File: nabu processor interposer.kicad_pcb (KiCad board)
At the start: 2 copper layers, 123 parts, among them IC1 Z80CPU-DIP-SOCKET, IC2 Aries 40-600-21, IC3 DMA-PLCC-44-CMOS, IC4 DMA-PLCC-44-CMOS, IC5 DMA-PLCC-44-CMOS, IC6 DMA-PLCC-44-CMOS, J1 5V EXTRA, J2 WRITE PROTECT, J3 USB HOST, J4 ETHERNET, U1 LP3963-3.3, U10 SST39SF040, U11 SST39SF040, U12 SST39SF040, U13 74AHC139, U14 74AHC139, U15 74LVC1G04, U16 74LVC1G02, U17 74LVC1G04, U18 74AHC273, U19 74HC245, U2 TXB0108DQSR, U20 74LVC1G32, U21 74LVC1G02, U22 74AHC273, U23 74HC245, U24 74LVC1G02, U25 74AHC273, U26 74HC245, U27 74LVC1G32, U28 74LVC1G02, U29 74AHC273, U3 TXB0108DQSR, U30 74HC245, U31 74LS153, U32 74LS153, U33 74LS153, U34 74LS153, U35 Teensy4.1, U36 TXB0108DQSR, U37 TXB0108DQSR, U38 74VHC9164FT, U39 74VHC9164FT, U4 TXB0108DQSR, U40 74VHC9164FT, U41 TXB0108DQSR, U42 TXB0108DQSR, U43 TXB0108DQSR, U44 74LS139, U45 74LVC1G32, U46 74HC245, U47 74LVC1G32, U48 74AHC273, U49 74HC74, U5 74LVC1G04, U50 74LS157, U51 74LS157, U52 74LS157, U53 74LS157, U54 74HC74, U55 74LS157, U56 74LS157, U57 74LS157, U58 74LS157, U59 74HC688, U6 TXB0108DQSR, U60 74AHC85, U61 74AHC85, U62 74AHC85, U63 74LVC1G10, U64 74LVC1G10, U65 74LVC1G332, U66 74LVC1G332, U67 74LVC1G04, U68 74LVC1G10, U69 74AHC85, U7 AS6C1616, U70 74LVC1G32, U71 74LVC1G04, U72 74AHC85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

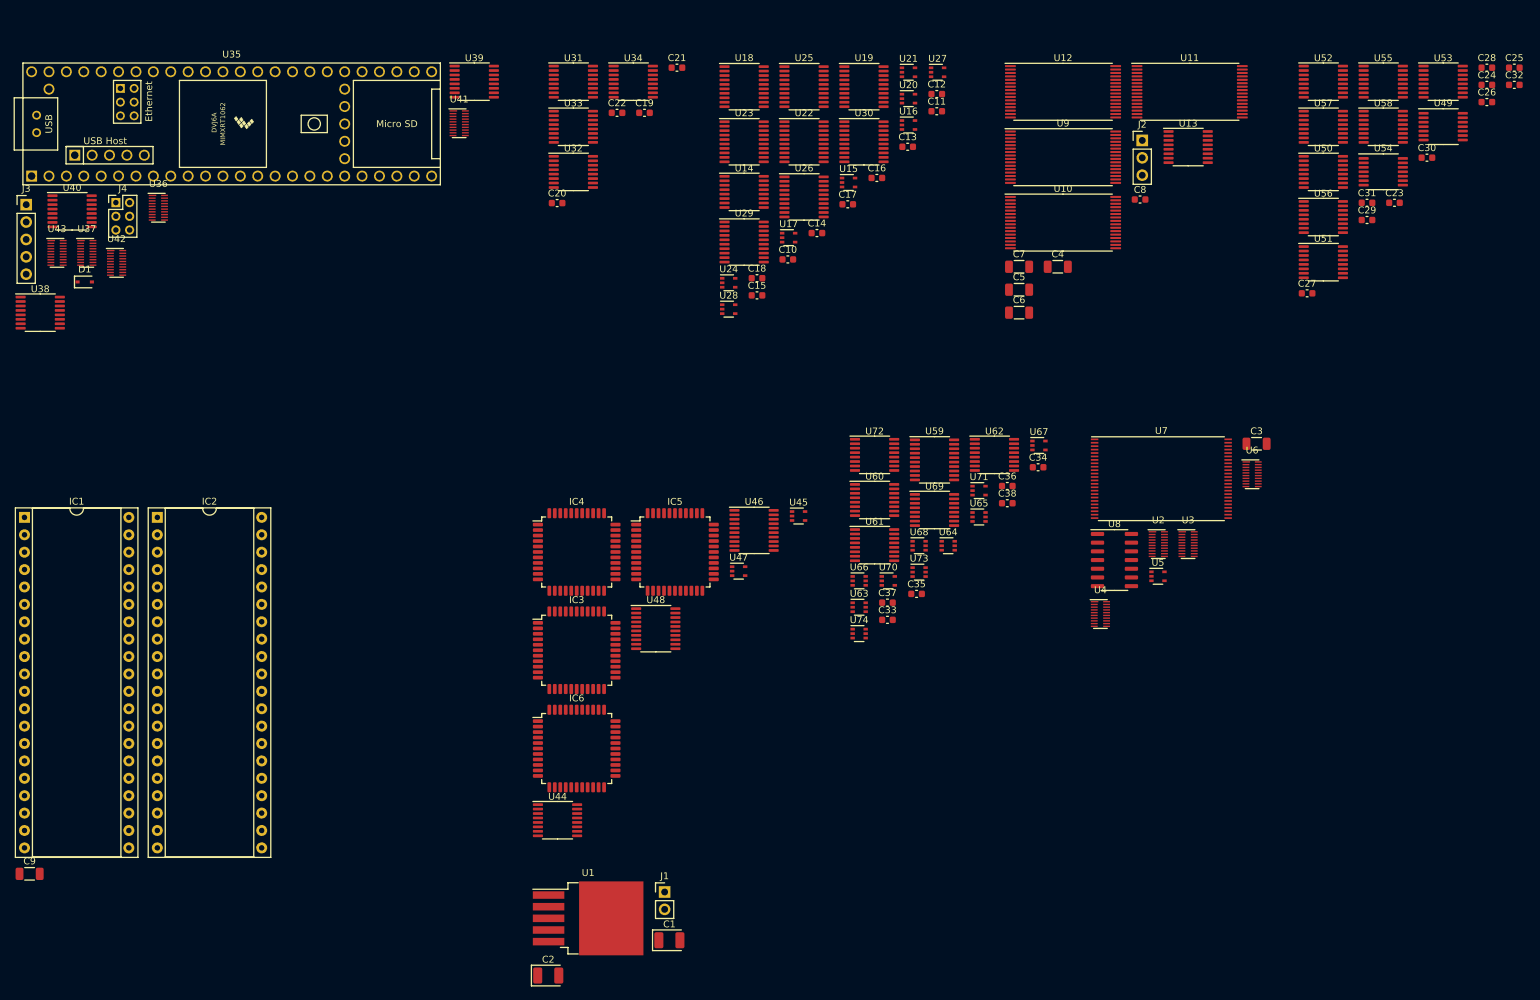
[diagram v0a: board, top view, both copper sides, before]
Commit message: updated 84c10 pinout, apparently never checked for validity.... further simplification of dma and timer system (removed mode 2 interrupt structure, and interrupts in general) cleaned up vhdl code for 1508, still need testing to ensure functionality and that it even fits in the 1508....
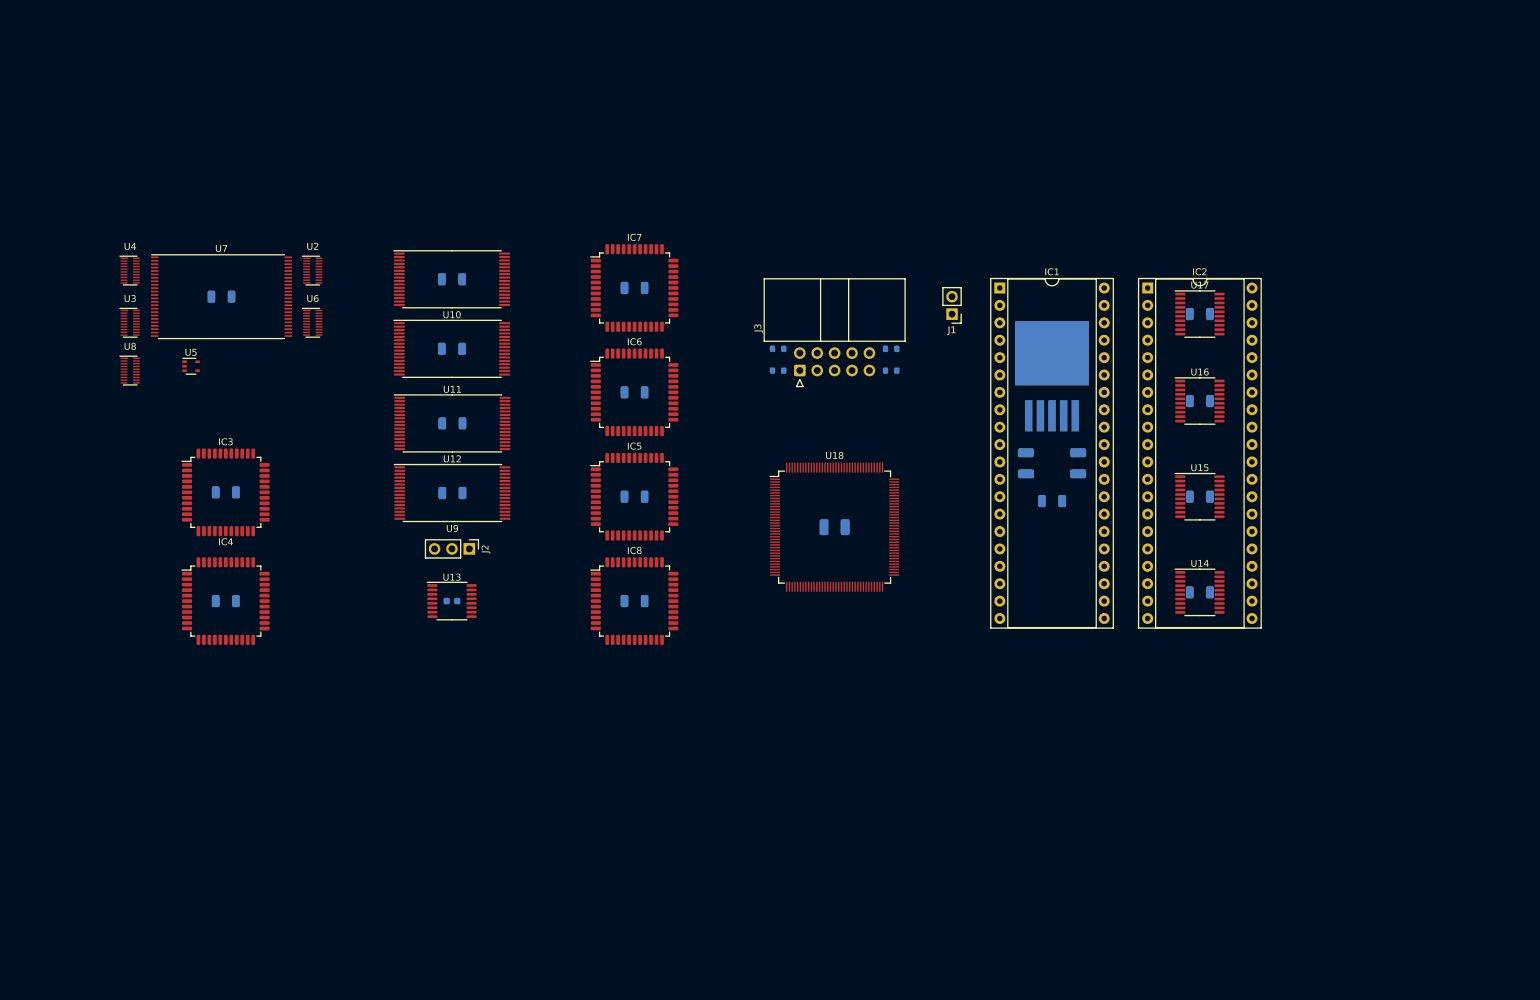
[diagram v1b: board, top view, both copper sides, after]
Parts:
- removed C21, C22, C23, C24, C25, C26, C27, C28, C29, C30, C31, C32, C33, C34, C35, C36, C37, C38: 0U1, Capacitor_SMD:C_0603_1608Metric
- removed D1: BAT48JFILM, Diode_SMD:D_SOD-323
- removed J4: ETHERNET, Connector_PinHeader_2.00mm:PinHeader_2x03_P2.00mm_Vertical
- removed U19, U23, U26, U30, U46: 74HC245, Package_SO:TSSOP-20_4.4x6.5mm_P0.65mm
- removed U20, U27, U45, U47, U70: 74LVC1G32, Package_TO_SOT_SMD:SOT-353_SC-70-5
- removed U21, U24, U28: 74LVC1G02, Package_TO_SOT_SMD:SOT-353_SC-70-5
- removed U22, U25, U29, U48: 74AHC273, Package_SO:TSSOP-20_4.4x6.5mm_P0.65mm
- removed U31, U32, U33, U34: 74LS153, Package_SO:TSSOP-16_4.4x5mm_P0.65mm
- removed U35: Teensy4.1, teensy:Teensy41
- removed U36, U37, U41, U42, U43: TXB0108DQSR, Package_SON:USON-20_2x4mm_P0.4mm
- removed U38, U39, U40: 74VHC9164FT, Package_SO:TSSOP-16_4.4x5mm_P0.65mm
- removed U44: 74LS139, Package_SO:TSSOP-16_4.4x5mm_P0.65mm
- removed U49, U54: 74HC74, Package_SO:TSSOP-14_4.4x5mm_P0.65mm
- removed U50, U51, U52, U53, U55, U56, U57, U58: 74LS157, Package_SO:TSSOP-16_4.4x5mm_P0.65mm
- removed U59: 74HC688, Package_SO:TSSOP-20_4.4x6.5mm_P0.65mm
- removed U60, U61, U62, U69, U72: 74AHC85, Package_SO:TSSOP-16_4.4x5mm_P0.65mm
- removed U63, U64, U68: 74LVC1G10, Package_TO_SOT_SMD:SOT-363_SC-70-6
- removed U65, U66, U73, U74: 74LVC1G332, Package_TO_SOT_SMD:SOT-363_SC-70-6
- removed U67, U71: 74LVC1G04, Package_TO_SOT_SMD:SOT-353_SC-70-5
- added IC7: DMA-PLCC-44-CMOS, Package_QFP:LQFP-44_10x10mm_P0.8mm, F.Cu at (134.6, 62.2)
- added IC8: DMA-PLCC-44-CMOS, Package_QFP:LQFP-44_10x10mm_P0.8mm, F.Cu at (134.6, 108.0)
- added R1: 4K7, Resistor_SMD:R_0603_1608Metric, B.Cu at (155.6, 74.3)
- added R2: 4K7, Resistor_SMD:R_0603_1608Metric, B.Cu at (172.1, 71.1)
- added R3: 4K7, Resistor_SMD:R_0603_1608Metric, B.Cu at (172.1, 74.3)
- added R4: 10K, Resistor_SMD:R_0603_1608Metric, B.Cu at (155.6, 71.1)
- C1, C2, C3, C4, C5, C6, C7, C8, U1: moved to B.Cu
- C10, C14, C15, C17, C18, C19, C20: value 0U1 -> 1U; footprint Capacitor_SMD:C_0603_1608Metric -> Capacitor_SMD:C_1206_3216Metric; moved to B.Cu
- C11, C12, C13: footprint Capacitor_SMD:C_0603_1608Metric -> Capacitor_SMD:C_1206_3216Metric; moved to B.Cu
- C16: value 0U1 -> 10U TANT; footprint Capacitor_SMD:C_0603_1608Metric -> Capacitor_Tantalum_SMD:CP_EIA-3528-15_AVX-H; moved to B.Cu
- C9: value 1U -> 0U1; moved to B.Cu
- IC1: value Z80CPU-DIP-SOCKET -> Aries 40-600-21
- IC2: value Aries 40-600-21 -> Z80CPU-DIP-SOCKET
- IC3, IC4: value DMA-PLCC-44-CMOS -> CTC-QFP-44
- J3: value USB HOST -> AVR-JTAG-10; footprint Connector_PinHeader_2.54mm:PinHeader_1x05_P2.54mm_Vertical -> Connector_IDC:IDC-Header_2x05_P2.54mm_Horizontal
- U14: value 74AHC139 -> 74HC245; footprint Package_SO:TSSOP-16_4.4x5mm_P0.65mm -> Package_SO:TSSOP-20_4.4x6.5mm_P0.65mm
- U15, U17: value 74LVC1G04 -> 74HC245; footprint Package_TO_SOT_SMD:SOT-353_SC-70-5 -> Package_SO:TSSOP-20_4.4x6.5mm_P0.65mm
- U16: value 74LVC1G02 -> 74HC245; footprint Package_TO_SOT_SMD:SOT-353_SC-70-5 -> Package_SO:TSSOP-20_4.4x6.5mm_P0.65mm
- U18: value 74AHC273 -> ATF1508-100; footprint Package_SO:TSSOP-20_4.4x6.5mm_P0.65mm -> Package_QFP:TQFP-144_16x16mm_P0.4mm
- U8: value TXB0104D -> TXB0108DQSR; footprint Package_SO:SOIC-14_3.9x8.7mm_P1.27mm -> Package_SON:USON-20_2x4mm_P0.4mm
- moved C9 175.8 mm to (217.2, 106.7), turned to 180 degrees
- moved U3 157.8 mm to (61.0, 67.3)
- moved C3 152.7 mm to (74.3, 63.5), turned to 180 degrees
- moved U4 150.3 mm to (61.0, 59.7)
- moved IC2 148.4 mm to (209.5, 62.2)
- moved U8 146.4 mm to (61.0, 74.3)
- moved IC1 146.3 mm to (188.0, 62.2)
- moved U5 144.5 mm to (69.8, 73.7)
- moved U7 139.8 mm to (74.3, 63.5)
- moved U6 138.9 mm to (87.6, 67.3)
- moved U2 129.8 mm to (87.6, 59.7)
- moved U13 126.3 mm to (108.0, 108.0)
- moved U11 118.1 mm to (108.0, 82.0)
- moved C8 116.3 mm to (108.0, 108.0), turned to 180 degrees
- moved J3 115.5 mm to (158.8, 74.3), turned to 90 degrees
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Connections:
- net /ROM/~{ROMEN0} renamed /ROM/~{ROM0}
- net /ROM/~{ROMEN_{1}} renamed /ROM/~{ROM_{1}}
- net /ROM/~{ROMEN_{2}} renamed /ROM/~{ROM_{2}}
- net /ROM/~{ROMEN_{3}} renamed /ROM/~{ROM_{3}}
- IC1 pad 1: /BRAINS/AB11 -> /BRAINS/XAB11
- IC1 pad 10: /BRAINS/DB6 -> /BRAINS/EDB6
- IC1 pad 12: /BRAINS/DB2 -> /BRAINS/EDB2
- IC1 pad 13: /BRAINS/DB7 -> /BRAINS/EDB7
- IC1 pad 14: /BRAINS/DB0 -> /BRAINS/EDB0
- IC1 pad 15: /BRAINS/DB1 -> /BRAINS/EDB1
- IC1 pad 17: unconnected-(IC1-Pad17) -> /BRAINS/~{NMI}
- IC1 pad 18: unconnected-(IC1-Pad18) -> /BRAINS/~{HALT}
- IC1 pad 19: /BRAINS/~{MREQ} -> /BRAINS/~{XMREQ}
- IC1 pad 2: /BRAINS/AB12 -> /BRAINS/XAB12
- IC1 pad 20: /BRAINS/~{IOREQ} -> /BRAINS/~{XIOREQ}
- IC1 pad 21: /BRAINS/~{RD} -> /BRAINS/~{XRD}
- IC1 pad 22: /BRAINS/~{WR} -> /BRAINS/~{XWR}
- IC1 pad 24: unconnected-(IC1-Pad24) -> /BRAINS/~{WAIT}
- IC1 pad 27: /BRAINS/~{M1} -> /BRAINS/~{XM1}
- IC1 pad 28: Net-(IC1-Pad28) -> /BRAINS/~{RFSH}
- IC1 pad 3: /BRAINS/AB13 -> /BRAINS/XAB13
- IC1 pad 30: /BRAINS/AB0 -> /BRAINS/XAB0
- IC1 pad 31: /BRAINS/AB1 -> /BRAINS/XAB1
- IC1 pad 32: /BRAINS/AB2 -> /BRAINS/XAB2
- IC1 pad 33: /BRAINS/AB3 -> /BRAINS/XAB3
- IC1 pad 34: /BRAINS/AB4 -> /BRAINS/XAB4
- IC1 pad 35: /BRAINS/AB5 -> /BRAINS/XAB5
- IC1 pad 36: /BRAINS/AB6 -> /BRAINS/XAB6
- IC1 pad 37: /BRAINS/AB7 -> /BRAINS/XAB7
- IC1 pad 38: /BRAINS/AB8 -> /BRAINS/XAB8
- IC1 pad 39: /BRAINS/AB9 -> /BRAINS/XAB9
- IC1 pad 4: /BRAINS/AB14 -> /BRAINS/XAB14
- IC1 pad 40: /BRAINS/AB10 -> /BRAINS/XAB10
- IC1 pad 5: /BRAINS/AB15 -> /BRAINS/XAB15
- IC1 pad 7: /BRAINS/DB4 -> /BRAINS/EDB4
- IC1 pad 8: /BRAINS/DB3 -> /BRAINS/EDB3
- IC1 pad 9: /BRAINS/DB5 -> /BRAINS/EDB5
- IC2 pad 28: Net-(IC1-Pad28) -> /BRAINS/~{RFSH}
- IC3 pad 1: /DECODE/AB5 -> /BRAINS/DB0
- IC3 pad 10: /DECODE/~{PORT_{4}RD} -> /BRAINS/DB6
- IC3 pad 11: /BRAINS/~{IOREQ} -> unconnected-(IC3-Pad11)
- IC3 pad 12: /BRAINS/~{RST} -> /BRAINS/DB7
- IC3 pad 13: +5V -> GND
- IC3 pad 14: /BRAINS/~{MREQ} -> /BRAINS/~{RD}
- IC3 pad 15: Net-(IC3-Pad15) -> unconnected-(IC3-Pad15)
- IC3 pad 16: /BRAINS/~{BUSAK} -> /DMA/RDY0
- IC3 pad 17: /BRAINS/~{BUSREQ} -> unconnected-(IC3-Pad17)
- IC3 pad 18: /DMA/~{DMASEL_{0}} -> /DMA/RDY1
- IC3 pad 19: /DECODE/AB15 -> Net-(IC3-Pad19)
- IC3 pad 2: /DECODE/AB4 -> /BRAINS/DB1
- IC3 pad 20: /DECODE/AB14 -> unconnected-(IC3-Pad20)
- IC3 pad 21: /DECODE/AB13 -> /BRAINS/~{IOREQ}
- IC3 pad 22: /DECODE/AB12 -> unconnected-(IC3-Pad22)
- IC3 pad 23: /DECODE/AB11 -> unconnected-(IC3-Pad23)
- IC3 pad 24: /DECODE/AB10 -> unconnected-(IC3-Pad24)
- IC3 pad 25: /DECODE/AB9 -> +5V
- IC3 pad 26: /DECODE/AB8 -> unconnected-(IC3-Pad26)
- IC3 pad 27: /DMA/DMARDY_{0} -> /BRAINS/~{M1}
- IC3 pad 29: unconnected-(IC3-Pad29) -> /BRAINS/CLK
- IC3 pad 3: /DECODE/AB3 -> /BRAINS/DB2
- IC3 pad 30: /BRAINS/~{M1} -> unconnected-(IC3-Pad30)
- IC3 pad 31: /DMA/DB7 -> /GLUE/~{TI0}
- IC3 pad 32: /DMA/DB5 -> /BRAINS/DB3
- IC3 pad 33: /DMA/DB6 -> /BRAINS/AB1
- IC3 pad 34: GND -> unconnected-(IC3-Pad34)
- IC3 pad 35: /DMA/DB4 -> /BRAINS/AB0
- IC3 pad 36: /DMA/DB3 -> Net-(IC3-Pad19)
- IC3 pad 37: /DMA/DB2 -> /BRAINS/CLK
- IC3 pad 38: /DMA/DB1 -> unconnected-(IC3-Pad38)
- IC3 pad 39: /DMA/DB0 -> unconnected-(IC3-Pad39)
- IC3 pad 4: /DECODE/AB2 -> /BRAINS/~{RST}
- IC3 pad 40: Net-(IC3-Pad40) -> /BRAINS/CLK
- IC3 pad 41: /BRAINS/~{INT} -> /BRAINS/CLK
- IC3 pad 42: (no net) -> unconnected-(IC3-Pad42)
- IC3 pad 43: /DECODE/AB7 -> +5V
- IC3 pad 44: /DECODE/AB6 -> unconnected-(IC3-Pad44)
- IC3 pad 5: /DECODE/AB1 -> unconnected-(IC3-Pad5)
- IC3 pad 6: (no net) -> unconnected-(IC3-Pad6)
- IC3 pad 7: /DECODE/AB0 -> unconnected-(IC3-Pad7)
- IC3 pad 8: /BRAINS/CLK -> /BRAINS/DB4
- IC3 pad 9: /DECODE/~{PORT_{4}WR} -> /BRAINS/DB5
- IC4 pad 1: /DECODE/AB5 -> /BRAINS/DB0
- IC4 pad 10: /DECODE/~{PORT_{4}RD} -> /BRAINS/DB6
- IC4 pad 11: /BRAINS/~{IOREQ} -> unconnected-(IC4-Pad11)
- IC4 pad 12: /BRAINS/~{RST} -> /BRAINS/DB7
- IC4 pad 13: +5V -> GND
- IC4 pad 14: /BRAINS/~{MREQ} -> /BRAINS/~{RD}
- IC4 pad 15: Net-(IC4-Pad15) -> unconnected-(IC4-Pad15)
- IC4 pad 16: Net-(IC3-Pad15) -> /DMA/RDY2
- IC4 pad 17: /BRAINS/~{BUSREQ} -> unconnected-(IC4-Pad17)
- IC4 pad 18: /DMA/~{DMASEL_{1}} -> /DMA/RDY3
- IC4 pad 19: /DECODE/AB15 -> Net-(IC4-Pad19)
- IC4 pad 2: /DECODE/AB4 -> /BRAINS/DB1
- IC4 pad 20: /DECODE/AB14 -> unconnected-(IC4-Pad20)
- IC4 pad 21: /DECODE/AB13 -> /BRAINS/~{IOREQ}
- IC4 pad 22: /DECODE/AB12 -> unconnected-(IC4-Pad22)
- IC4 pad 23: /DECODE/AB11 -> unconnected-(IC4-Pad23)
- IC4 pad 24: /DECODE/AB10 -> unconnected-(IC4-Pad24)
- IC4 pad 25: /DECODE/AB9 -> +5V
- IC4 pad 26: /DECODE/AB8 -> unconnected-(IC4-Pad26)
- IC4 pad 27: /DMA/DMARDY_{1} -> /BRAINS/~{M1}
- IC4 pad 29: unconnected-(IC4-Pad29) -> /BRAINS/CLK
- IC4 pad 3: /DECODE/AB3 -> /BRAINS/DB2
- IC4 pad 30: /BRAINS/~{M1} -> unconnected-(IC4-Pad30)
- IC4 pad 31: /DMA/DB7 -> /GLUE/~{TI1}
- IC4 pad 32: /DMA/DB5 -> /BRAINS/DB3
- IC4 pad 33: /DMA/DB6 -> /BRAINS/AB1
- IC4 pad 34: GND -> unconnected-(IC4-Pad34)
- IC4 pad 35: /DMA/DB4 -> /BRAINS/AB0
- IC4 pad 36: /DMA/DB3 -> Net-(IC4-Pad19)
- IC4 pad 37: /DMA/DB2 -> /BRAINS/CLK
- IC4 pad 38: /DMA/DB1 -> unconnected-(IC4-Pad38)
- IC4 pad 39: /DMA/DB0 -> unconnected-(IC4-Pad39)
- IC4 pad 4: /DECODE/AB2 -> /BRAINS/~{RST}
- IC4 pad 40: Net-(IC4-Pad40) -> /BRAINS/CLK
- IC4 pad 41: /BRAINS/~{INT} -> /BRAINS/CLK
- IC4 pad 42: (no net) -> unconnected-(IC4-Pad42)
- IC4 pad 43: /DECODE/AB7 -> +5V
- IC4 pad 44: /DECODE/AB6 -> unconnected-(IC4-Pad44)
- IC4 pad 5: /DECODE/AB1 -> unconnected-(IC4-Pad5)
- IC4 pad 6: (no net) -> unconnected-(IC4-Pad6)
- IC4 pad 7: /DECODE/AB0 -> unconnected-(IC4-Pad7)
- IC4 pad 8: /BRAINS/CLK -> /BRAINS/DB4
- IC4 pad 9: /DECODE/~{PORT_{4}WR} -> /BRAINS/DB5
- IC5 pad 1: /DECODE/AB5 -> /BRAINS/AB5
- IC5 pad 10: /DECODE/~{PORT_{4}RD} -> /BRAINS/~{RD}
- IC5 pad 16: Net-(IC4-Pad15) -> /BRAINS/~{BUSAK}
- IC5 pad 18: /DMA/~{DMASEL_{2}} -> /DMA/~{DMASEL_{0}}
- IC5 pad 19: /DECODE/AB15 -> /BRAINS/AB15
- IC5 pad 2: /DECODE/AB4 -> /BRAINS/AB4
- IC5 pad 20: /DECODE/AB14 -> /BRAINS/AB14
- IC5 pad 21: /DECODE/AB13 -> /BRAINS/AB13
- IC5 pad 22: /DECODE/AB12 -> /BRAINS/AB12
- IC5 pad 23: /DECODE/AB11 -> /BRAINS/AB11
- IC5 pad 24: /DECODE/AB10 -> /BRAINS/AB10
- IC5 pad 25: /DECODE/AB9 -> /BRAINS/AB9
- IC5 pad 26: /DECODE/AB8 -> /BRAINS/AB8
- IC5 pad 27: /DMA/DMARDY_{2} -> /DMA/RDY0
- IC5 pad 3: /DECODE/AB3 -> /BRAINS/AB3
- IC5 pad 31: /DMA/DB7 -> /BRAINS/DB7
- IC5 pad 32: /DMA/DB5 -> /BRAINS/DB6
- IC5 pad 33: /DMA/DB6 -> /BRAINS/DB5
- IC5 pad 35: /DMA/DB4 -> /BRAINS/DB4
- IC5 pad 36: /DMA/DB3 -> /BRAINS/DB3
- IC5 pad 37: /DMA/DB2 -> /BRAINS/DB2
- IC5 pad 38: /DMA/DB1 -> /BRAINS/DB1
- IC5 pad 39: /DMA/DB0 -> /BRAINS/DB0
- IC5 pad 4: /DECODE/AB2 -> /BRAINS/AB2
- IC5 pad 40: Net-(IC5-Pad40) -> unconnected-(IC5-Pad40)
- IC5 pad 41: /BRAINS/~{INT} -> unconnected-(IC5-Pad41)
- IC5 pad 42: (no net) -> +5V
- IC5 pad 43: /DECODE/AB7 -> /BRAINS/AB7
- IC5 pad 44: /DECODE/AB6 -> /BRAINS/AB6
- IC5 pad 5: /DECODE/AB1 -> /BRAINS/AB1
- IC5 pad 7: /DECODE/AB0 -> /BRAINS/AB0
- IC5 pad 9: /DECODE/~{PORT_{4}WR} -> /BRAINS/~{WR}
- IC6 pad 1: /DECODE/AB5 -> /BRAINS/AB5
- IC6 pad 10: /DECODE/~{PORT_{4}RD} -> /BRAINS/~{RD}
- IC6 pad 15: unconnected-(IC6-Pad15) -> Net-(IC6-Pad15)
- IC6 pad 18: /DMA/~{DMASEL_{3}} -> /DMA/~{DMASEL_{1}}
- IC6 pad 19: /DECODE/AB15 -> /BRAINS/AB15
- IC6 pad 2: /DECODE/AB4 -> /BRAINS/AB4
- IC6 pad 20: /DECODE/AB14 -> /BRAINS/AB14
- IC6 pad 21: /DECODE/AB13 -> /BRAINS/AB13
- IC6 pad 22: /DECODE/AB12 -> /BRAINS/AB12
- IC6 pad 23: /DECODE/AB11 -> /BRAINS/AB11
- IC6 pad 24: /DECODE/AB10 -> /BRAINS/AB10
- IC6 pad 25: /DECODE/AB9 -> /BRAINS/AB9
- IC6 pad 26: /DECODE/AB8 -> /BRAINS/AB8
- IC6 pad 27: /DMA/DMARDY_{3} -> /DMA/RDY1
- IC6 pad 3: /DECODE/AB3 -> /BRAINS/AB3
- IC6 pad 31: /DMA/DB7 -> /BRAINS/DB7
- IC6 pad 32: /DMA/DB5 -> /BRAINS/DB6
- IC6 pad 33: /DMA/DB6 -> /BRAINS/DB5
- IC6 pad 35: /DMA/DB4 -> /BRAINS/DB4
- IC6 pad 36: /DMA/DB3 -> /BRAINS/DB3
- IC6 pad 37: /DMA/DB2 -> /BRAINS/DB2
- IC6 pad 38: /DMA/DB1 -> /BRAINS/DB1
- IC6 pad 39: /DMA/DB0 -> /BRAINS/DB0
- IC6 pad 4: /DECODE/AB2 -> /BRAINS/AB2
- IC6 pad 41: /BRAINS/~{INT} -> unconnected-(IC6-Pad41)
- IC6 pad 42: (no net) -> +5V
- IC6 pad 43: /DECODE/AB7 -> /BRAINS/AB7
- IC6 pad 44: /DECODE/AB6 -> /BRAINS/AB6
- IC6 pad 5: /DECODE/AB1 -> /BRAINS/AB1
- IC6 pad 7: /DECODE/AB0 -> /BRAINS/AB0
- IC6 pad 9: /DECODE/~{PORT_{4}WR} -> /BRAINS/~{WR}
- J2 pad 1: /BRAINS/~{WR} -> /RAM/~{WR}
- J3 pad 1: Net-(J3-Pad1) -> /GLUE/TCK
- J3 pad 2: Net-(J3-Pad2) -> GND
- J3 pad 3: Net-(J3-Pad3) -> /GLUE/TDO
- J3 pad 4: GND -> +5V
- J3 pad 5: GND -> /GLUE/TMS
- U10 pad 1: /MUX/EAB18 -> /GLUE/EAB18
- U10 pad 10: /MUX/AB2 -> /GLUE/EAB2
- U10 pad 11: /MUX/AB1 -> /GLUE/EAB1
- U10 pad 12: /MUX/AB0 -> /GLUE/EAB0
- U10 pad 13: /DEV PORT/DB0 -> /BRAINS/DB0
- U10 pad 14: /DEV PORT/DB1 -> /BRAINS/DB1
- U10 pad 15: /DEV PORT/DB2 -> /BRAINS/DB2
- U10 pad 17: /DEV PORT/DB3 -> /BRAINS/DB3
- U10 pad 18: /DEV PORT/DB4 -> /BRAINS/DB4
- U10 pad 19: /DEV PORT/DB5 -> /BRAINS/DB5
- U10 pad 2: /MUX/EAB16 -> /GLUE/EAB16
- U10 pad 20: /DEV PORT/DB6 -> /BRAINS/DB6
- U10 pad 21: /DEV PORT/DB7 -> /BRAINS/DB7
- U10 pad 23: /MUX/AB10 -> /GLUE/EAB10
- U10 pad 24: /BRAINS/~{RD} -> /RAM/~{RD}
- U10 pad 25: /MUX/AB11 -> /GLUE/EAB11
- U10 pad 26: /MUX/AB9 -> /GLUE/EAB9
- U10 pad 27: /MUX/AB8 -> /GLUE/EAB8
- U10 pad 28: /MUX/AB13 -> /GLUE/EAB13
- U10 pad 29: /MUX/EAB14 -> /GLUE/EAB14
- U10 pad 3: /MUX/EAB15 -> /GLUE/EAB15
- U10 pad 30: /MUX/EAB17 -> /GLUE/EAB17
- U10 pad 4: /MUX/AB12 -> /GLUE/EAB12
- U10 pad 5: /MUX/AB7 -> /GLUE/EAB7
- U10 pad 6: /MUX/AB6 -> /GLUE/EAB6
- U10 pad 7: /MUX/AB5 -> /GLUE/EAB5
- U10 pad 8: /MUX/AB4 -> /GLUE/EAB4
- U10 pad 9: /MUX/AB3 -> /GLUE/EAB3
- U11 pad 1: /MUX/EAB18 -> /GLUE/EAB18
- U11 pad 10: /MUX/AB2 -> /GLUE/EAB2
- U11 pad 11: /MUX/AB1 -> /GLUE/EAB1
- U11 pad 12: /MUX/AB0 -> /GLUE/EAB0
- U11 pad 13: /DEV PORT/DB0 -> /BRAINS/DB0
- U11 pad 14: /DEV PORT/DB1 -> /BRAINS/DB1
- U11 pad 15: /DEV PORT/DB2 -> /BRAINS/DB2
- U11 pad 17: /DEV PORT/DB3 -> /BRAINS/DB3
- U11 pad 18: /DEV PORT/DB4 -> /BRAINS/DB4
- U11 pad 19: /DEV PORT/DB5 -> /BRAINS/DB5
- U11 pad 2: /MUX/EAB16 -> /GLUE/EAB16
- U11 pad 20: /DEV PORT/DB6 -> /BRAINS/DB6
- U11 pad 21: /DEV PORT/DB7 -> /BRAINS/DB7
- U11 pad 23: /MUX/AB10 -> /GLUE/EAB10
- U11 pad 24: /BRAINS/~{RD} -> /RAM/~{RD}
- U11 pad 25: /MUX/AB11 -> /GLUE/EAB11
- U11 pad 26: /MUX/AB9 -> /GLUE/EAB9
- U11 pad 27: /MUX/AB8 -> /GLUE/EAB8
- U11 pad 28: /MUX/AB13 -> /GLUE/EAB13
- U11 pad 29: /MUX/EAB14 -> /GLUE/EAB14
- U11 pad 3: /MUX/EAB15 -> /GLUE/EAB15
- U11 pad 30: /MUX/EAB17 -> /GLUE/EAB17
- U11 pad 4: /MUX/AB12 -> /GLUE/EAB12
- U11 pad 5: /MUX/AB7 -> /GLUE/EAB7
- U11 pad 6: /MUX/AB6 -> /GLUE/EAB6
- U11 pad 7: /MUX/AB5 -> /GLUE/EAB5
- U11 pad 8: /MUX/AB4 -> /GLUE/EAB4
- U11 pad 9: /MUX/AB3 -> /GLUE/EAB3
- U12 pad 1: /MUX/EAB18 -> /GLUE/EAB18
- U12 pad 10: /MUX/AB2 -> /GLUE/EAB2
- U12 pad 11: /MUX/AB1 -> /GLUE/EAB1
- U12 pad 12: /MUX/AB0 -> /GLUE/EAB0
- U12 pad 13: /DEV PORT/DB0 -> /BRAINS/DB0
- U12 pad 14: /DEV PORT/DB1 -> /BRAINS/DB1
- U12 pad 15: /DEV PORT/DB2 -> /BRAINS/DB2
- U12 pad 17: /DEV PORT/DB3 -> /BRAINS/DB3
- U12 pad 18: /DEV PORT/DB4 -> /BRAINS/DB4
- U12 pad 19: /DEV PORT/DB5 -> /BRAINS/DB5
- U12 pad 2: /MUX/EAB16 -> /GLUE/EAB16
- U12 pad 20: /DEV PORT/DB6 -> /BRAINS/DB6
- U12 pad 21: /DEV PORT/DB7 -> /BRAINS/DB7
- U12 pad 23: /MUX/AB10 -> /GLUE/EAB10
- U12 pad 24: /BRAINS/~{RD} -> /RAM/~{RD}
- U12 pad 25: /MUX/AB11 -> /GLUE/EAB11
- U12 pad 26: /MUX/AB9 -> /GLUE/EAB9
- U12 pad 27: /MUX/AB8 -> /GLUE/EAB8
- U12 pad 28: /MUX/AB13 -> /GLUE/EAB13
- U12 pad 29: /MUX/EAB14 -> /GLUE/EAB14
- U12 pad 3: /MUX/EAB15 -> /GLUE/EAB15
- U12 pad 30: /MUX/EAB17 -> /GLUE/EAB17
- U12 pad 4: /MUX/AB12 -> /GLUE/EAB12
- U12 pad 5: /MUX/AB7 -> /GLUE/EAB7
- U12 pad 6: /MUX/AB6 -> /GLUE/EAB6
- U12 pad 7: /MUX/AB5 -> /GLUE/EAB5
- U12 pad 8: /MUX/AB4 -> /GLUE/EAB4
- U12 pad 9: /MUX/AB3 -> /GLUE/EAB3
- U13 pad 1: /DECODE/~{ROMEN} -> /GLUE/~{ROM}
- U13 pad 10: unconnected-(U13-Pad10) -> /DMA/~{DMASEL_{2}}
- U13 pad 11: unconnected-(U13-Pad11) -> /DMA/~{DMASEL_{1}}
- U13 pad 12: unconnected-(U13-Pad12) -> /DMA/~{DMASEL_{0}}
- U13 pad 13: GND -> /BRAINS/AB1
- U13 pad 14: GND -> /BRAINS/AB0
- U13 pad 15: +5V -> /DMA/~{DMA}
- U13 pad 2: /MUX/EAB20 -> /GLUE/EAB20
- U13 pad 3: /MUX/EAB19 -> /GLUE/EAB19
- U13 pad 9: unconnected-(U13-Pad9) -> /DMA/~{DMASEL_{3}}
- U14 pad 1: Net-(U14-Pad1) -> GND
- U14 pad 10: /MAPPER/~{MAPRD_{2}} -> GND
- U14 pad 11: /MAPPER/~{MAPRD_{1}} -> unconnected-(U14-Pad11)
- U14 pad 12: /MAPPER/~{MAPRD_{0}} -> unconnected-(U14-Pad12)
- U14 pad 13: /MAPPER/AB0 -> unconnected-(U14-Pad13)
- U14 pad 14: /MAPPER/AB1 -> /BRAINS/~{WR}
- U14 pad 15: Net-(U14-Pad15) -> /BRAINS/~{RD}
- U14 pad 16: +5V -> /BRAINS/~{IOREQ}
- U14 pad 2: /MAPPER/AB1 -> /BRAINS/~{XM1}
- U14 pad 3: /MAPPER/AB0 -> /BRAINS/~{XMREQ}
- U14 pad 4: /MAPPER/~{MAPWR_{0}} -> /BRAINS/~{XIOREQ}
- U14 pad 5: /MAPPER/~{MAPWR_{1}} -> /BRAINS/~{XRD}
- U14 pad 6: /MAPPER/~{MAPWR_{2}} -> /BRAINS/~{XWR}
- U14 pad 7: /MAPPER/~{MAPWR_{3}} -> unconnected-(U14-Pad7)
- U14 pad 8: GND -> unconnected-(U14-Pad8)
- U14 pad 9: /MAPPER/~{MAPRD_{3}} -> unconnected-(U14-Pad9)
- U15 pad 1: (no net) -> GND
- U15 pad 2: /BRAINS/~{RST} -> /BRAINS/EDB0
- U15 pad 3: GND -> /BRAINS/EDB1
- U15 pad 4: Net-(U15-Pad4) -> /BRAINS/EDB2
- U15 pad 5: +5V -> /BRAINS/EDB3
- U16 pad 1: /MAPPER/~{MAPWR_{0}} -> GND
- U16 pad 2: Net-(U15-Pad4) -> /BRAINS/XAB0
- U16 pad 3: GND -> /BRAINS/XAB1
- U16 pad 4: Net-(U16-Pad4) -> /BRAINS/XAB2
- U16 pad 5: +5V -> /BRAINS/XAB3
- U17 pad 1: (no net) -> GND
- U17 pad 2: Net-(U15-Pad4) -> /BRAINS/XAB8
- U17 pad 3: GND -> /BRAINS/XAB9
- U17 pad 4: Net-(U17-Pad4) -> /BRAINS/XAB10
- U17 pad 5: +5V -> /BRAINS/XAB11
- U18 pad 1: Net-(U17-Pad4) -> unconnected-(U18-Pad1)
- U18 pad 10: GND -> /BRAINS/DB6
- U18 pad 11: Net-(U16-Pad4) -> GND
- U18 pad 12: /MAPPER/PAB_{1}4 -> /BRAINS/DB7
- U18 pad 13: /MAPPER/DB4 -> unconnected-(U18-Pad13)
- U18 pad 14: /MAPPER/DB5 -> unconnected-(U18-Pad14)
- U18 pad 15: /MAPPER/PAB_{1}5 -> /GLUE/TMS
- U18 pad 16: /MAPPER/PAB_{1}6 -> unconnected-(U18-Pad16)
- U18 pad 17: /MAPPER/DB6 -> /GLUE/EAB14
- U18 pad 18: /MAPPER/DB7 -> +5V
- U18 pad 19: /MAPPER/PAB_{1}7 -> /GLUE/EAB15
- U18 pad 2: /MAPPER/PAB_{1}0 -> /BRAINS/DB0
- U18 pad 20: +5V -> /GLUE/EAB16
- U18 pad 3: /MAPPER/DB0 -> +5V
- U18 pad 4: /MAPPER/DB1 -> /GLUE/TDI
- U18 pad 5: /MAPPER/PAB_{1}1 -> /BRAINS/DB1
- U18 pad 6: /MAPPER/PAB_{1}2 -> /BRAINS/DB2
- U18 pad 7: /MAPPER/DB2 -> /BRAINS/DB3
- U18 pad 8: /MAPPER/DB3 -> /BRAINS/DB4
- U18 pad 9: /MAPPER/PAB_{1}3 -> /BRAINS/DB5
- U2 pad 11: /DEV PORT/DB7 -> /BRAINS/DB7
- U2 pad 12: /DEV PORT/DB6 -> /BRAINS/DB6
- U2 pad 13: /DEV PORT/DB5 -> /BRAINS/DB5
- U2 pad 14: /DEV PORT/DB4 -> /BRAINS/DB4
- U2 pad 17: /DEV PORT/DB3 -> /BRAINS/DB3
- U2 pad 18: /DEV PORT/DB2 -> /BRAINS/DB2
- U2 pad 19: /DEV PORT/DB1 -> /BRAINS/DB1
- U2 pad 20: /DEV PORT/DB0 -> /BRAINS/DB0
- U3 pad 11: /MUX/AB7 -> /GLUE/EAB7
- U3 pad 12: /MUX/AB6 -> /GLUE/EAB6
- U3 pad 13: /MUX/AB5 -> /GLUE/EAB5
- U3 pad 14: /MUX/AB4 -> /GLUE/EAB4
- U3 pad 17: /MUX/AB3 -> /GLUE/EAB3
- U3 pad 18: /MUX/AB2 -> /GLUE/EAB2
- U3 pad 19: /MUX/AB1 -> /GLUE/EAB1
- U3 pad 20: /MUX/AB0 -> /GLUE/EAB0
- U4 pad 11: /MUX/EAB15 -> /GLUE/EAB15
- U4 pad 12: /MUX/EAB14 -> /GLUE/EAB14
- U4 pad 13: /MUX/AB13 -> /GLUE/EAB13
- U4 pad 14: /MUX/AB12 -> /GLUE/EAB12
- U4 pad 17: /MUX/AB11 -> /GLUE/EAB11
- U4 pad 18: /MUX/AB10 -> /GLUE/EAB10
- U4 pad 19: /MUX/AB9 -> /GLUE/EAB9
- U4 pad 20: /MUX/AB8 -> /GLUE/EAB8
- U6 pad 14: /MUX/EAB20 -> /GLUE/EAB20
- U6 pad 17: /MUX/EAB19 -> /GLUE/EAB19
- U6 pad 18: /MUX/EAB18 -> /GLUE/EAB18
- U6 pad 19: /MUX/EAB17 -> /GLUE/EAB17
- U6 pad 20: /MUX/EAB16 -> /GLUE/EAB16
- U8 pad 1: +3V3 -> Net-(U7-Pad28)
- U8 pad 11: /DECODE/~{RAMEN} -> GND
- U8 pad 12: /BRAINS/~{WR} -> GND
- U8 pad 13: /BRAINS/~{RD} -> GND
- U8 pad 14: +5V -> GND
- U8 pad 2: Net-(U7-Pad28) -> Net-(U7-Pad11)
- U8 pad 3: Net-(U7-Pad11) -> Net-(U7-Pad26)
- U8 pad 4: Net-(U7-Pad26) -> GND
- U8 pad 5: GND -> +3V3
- U8 pad 6: unconnected-(U8-Pad6) -> +3V3
- U8 pad 8: +3V3 -> GND
- U8 pad 9: unconnected-(U8-Pad9) -> GND
- U9 pad 1: /MUX/EAB18 -> /GLUE/EAB18
- U9 pad 10: /MUX/AB2 -> /GLUE/EAB2
- U9 pad 11: /MUX/AB1 -> /GLUE/EAB1
- U9 pad 12: /MUX/AB0 -> /GLUE/EAB0
- U9 pad 13: /DEV PORT/DB0 -> /BRAINS/DB0
- U9 pad 14: /DEV PORT/DB1 -> /BRAINS/DB1
- U9 pad 15: /DEV PORT/DB2 -> /BRAINS/DB2
- U9 pad 17: /DEV PORT/DB3 -> /BRAINS/DB3
- U9 pad 18: /DEV PORT/DB4 -> /BRAINS/DB4
- U9 pad 19: /DEV PORT/DB5 -> /BRAINS/DB5
- U9 pad 2: /MUX/EAB16 -> /GLUE/EAB16
- U9 pad 20: /DEV PORT/DB6 -> /BRAINS/DB6
- U9 pad 21: /DEV PORT/DB7 -> /BRAINS/DB7
- U9 pad 23: /MUX/AB10 -> /GLUE/EAB10
- U9 pad 24: /BRAINS/~{RD} -> /RAM/~{RD}
- U9 pad 25: /MUX/AB11 -> /GLUE/EAB11
- U9 pad 26: /MUX/AB9 -> /GLUE/EAB9
- U9 pad 27: /MUX/AB8 -> /GLUE/EAB8
- U9 pad 28: /MUX/AB13 -> /GLUE/EAB13
- U9 pad 29: /MUX/EAB14 -> /GLUE/EAB14
- U9 pad 3: /MUX/EAB15 -> /GLUE/EAB15
- U9 pad 30: /MUX/EAB17 -> /GLUE/EAB17
- U9 pad 4: /MUX/AB12 -> /GLUE/EAB12
- U9 pad 5: /MUX/AB7 -> /GLUE/EAB7
- U9 pad 6: /MUX/AB6 -> /GLUE/EAB6
- U9 pad 7: /MUX/AB5 -> /GLUE/EAB5
- U9 pad 8: /MUX/AB4 -> /GLUE/EAB4
- U9 pad 9: /MUX/AB3 -> /GLUE/EAB3

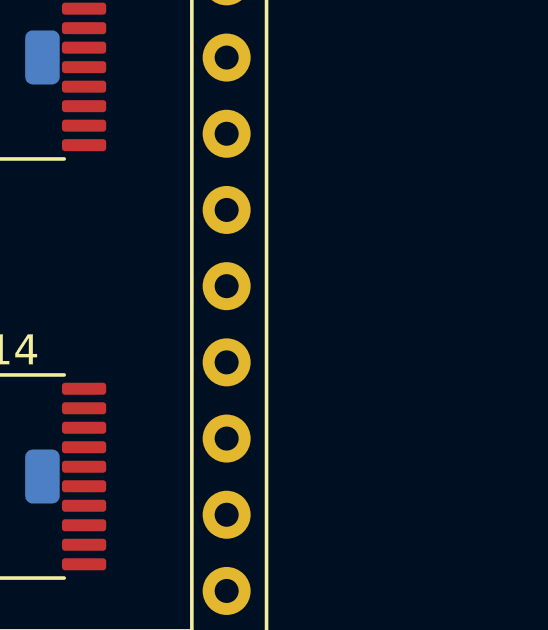
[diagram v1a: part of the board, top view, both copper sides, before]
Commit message: Added R5: a pull-up resistor for the /BUSREQ pin
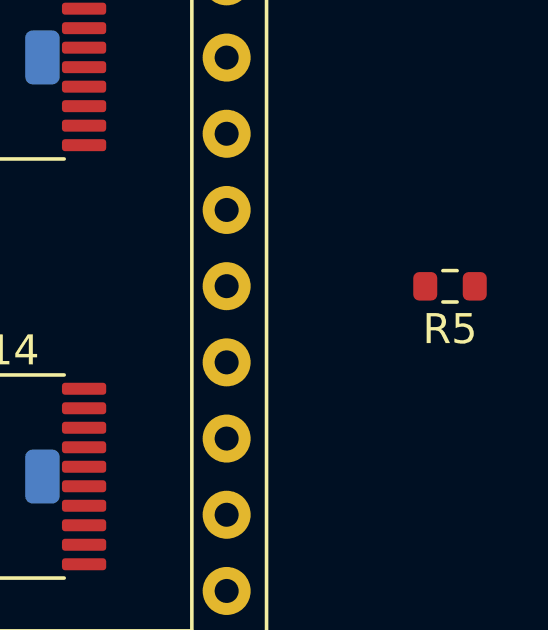
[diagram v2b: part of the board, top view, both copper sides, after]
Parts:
- added R5: 10k, Resistor_SMD:R_0603_1608Metric, F.Cu at (232.2, 100.3)
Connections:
- U15 pad 1: GND -> /BRAINS/DIR
- U18 pad 83: unconnected-(U18-Pad83) -> /BRAINS/DIR
- U18 pad 93: unconnected-(U18-Pad93) -> /BRAINS/~{M1}
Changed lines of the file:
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@@
   (net 234 "unconnected-(U18-Pad55)")
   (net 235 "unconnected-(U18-Pad56)")
-  (net 236 "unconnected-(U18-Pad83)")
+  (net 236 "/BRAINS/DIR")
   (net 237 "unconnected-(U18-Pad84)")
   (net 238 "unconnected-(U18-Pad85)")
@@
   (net 242 "unconnected-(U18-Pad90)")
   (net 243 "unconnected-(U18-Pad92)")
-  (net 244 "unconnected-(U18-Pad93)")
   (footprint "Connector_PinHeader_2.54mm:PinHeader_1x03_P2.54mm_Vertical" (layer "F.Cu")
     (at 110.49 100.33 -90)
@@
       (net 1 "+5V") (pinfunction "VCC") (pintype "power_in"))
     (model "${KICAD6_3DMODEL_DIR}/Package_SO.3dshapes/TSOP-I-32_14.4x8mm_P0.5mm.wrl"
+      (offset (xyz 0 0 0))
+      (scale (xyz 1 1 1))
+      (rotate (xyz 0 0 0))
+    )
+  )
+  (footprint "Resistor_SMD:R_0603_1608Metric" (layer "F.Cu")
+    (at 232.23 100.34 180)
+    (descr "Resistor SMD 0603 (1608 Metric), square (rectangular) end terminal, IPC_7351 nominal, (Body size source: IPC-SM-782 page 72, https://www.pcb-3d.com/wordpress/wp-content/uploads/ipc-sm-782a_amendment_1_and_2.pdf), generated with kicad-footprint-generator")
+    (tags "resistor")
+    (property "Sheetfile" "BRAINS.kicad_sch")
+    (property "Sheetname" "BRAINS")
+    (attr smd)
+    (fp_text reference "R5" (at 0 -1.43) (layer "F.SilkS")
+      (effects (font (size 1 1) (thickness 0.15)))
+    )
+    (fp_text value "10k" (at 0 1.43) (layer "F.Fab")
+      (effects (font (size 1 1) (thickness 0.15)))
+    )
+    (fp_text user "${REFERENCE}" (at 0 0) (layer "F.Fab")
+      (effects (font (size 0.4 0.4) (thickness 0.06)))
+    )
+    (fp_line (start -0.237258 0.5225) (end 0.237258 0.5225) (layer "F.SilkS") (width 0.12))
+    (fp_line (start -0.237258 -0.5225) (end 0.237258 -0.5225) (layer "F.SilkS") (width 0.12))
+    (fp_line (start 1.48 -0.73) (end 1.48 0.73) (layer "F.CrtYd") (width 0.05))
+    (fp_line (start -1.48 0.73) (end -1.48 -0.73) (layer "F.CrtYd") (width 0.05))
+    (fp_line (start -1.48 -0.73) (end 1.48 -0.73) (layer "F.CrtYd") (width 0.05))
+    (fp_line (start 1.48 0.73) (end -1.48 0.73) (layer "F.CrtYd") (width 0.05))
+    (fp_line (start 0.8 0.4125) (end -0.8 0.4125) (layer "F.Fab") (width 0.1))
+    (fp_line (start -0.8 0.4125) (end -0.8 -0.4125) (layer "F.Fab") (width 0.1))
+    (fp_line (start 0.8 -0.4125) (end 0.8 0.4125) (layer "F.Fab") (width 0.1))
+    (fp_line (start -0.8 -0.4125) (end 0.8 -0.4125) (layer "F.Fab") (width 0.1))
+    (pad "1" smd roundrect (at -0.825 0 180) (size 0.8 0.95) (layers "F.Cu" "F.Paste" "F.Mask") (roundrect_rratio 0.25)
+      (net 1 "+5V") (pintype "passive"))
+    (pad "2" smd roundrect (at 0.825 0 180) (size 0.8 0.95) (layers "F.Cu" "F.Paste" "F.Mask") (roundrect_rratio 0.25)
+      (net 45 "/BRAINS/~{BUSREQ}") (pintype "passive"))
+    (model "${KICAD6_3DMODEL_DIR}/Resistor_SMD.3dshapes/R_0603_1608Metric.wrl"
       (offset (xyz 0 0 0))
       (scale (xyz 1 1 1))
@@
       (net 1 "+5V") (pinfunction "VCCIO") (pintype "power_in"))
     (pad "83" smd rect (at 8.7 3) (size 1.45 0.2) (layers "F.Cu" "F.Paste" "F.Mask")
-      (net 236 "unconnected-(U18-Pad83)") (pinfunction "IO") (pintype "bidirectional+no_connect"))
+      (net 236 "/BRAINS/DIR") (pinfunction "IO") (pintype "bidirectional"))
     (pad "84" smd rect (at 8.7 2.6) (size 1.45 0.2) (layers "F.Cu" "F.Paste" "F.Mask")
       (net 237 "unconnected-(U18-Pad84)") (pinfunction "IO") (pintype "bidirectional+no_connect"))
@@
       (net 243 "unconnected-(U18-Pad92)") (pinfunction "IO") (pintype "bidirectional+no_connect"))
     (pad "93" smd rect (at 8.7 -1) (size 1.45 0.2) (layers "F.Cu" "F.Paste" "F.Mask")
-      (net 244 "unconnected-(U18-Pad93)") (pinfunction "IO") (pintype "bidirectional+no_connect"))
+      (net 28 "/BRAINS/~{M1}") (pinfunction "IO") (pintype "bidirectional"))
     (pad "94" smd rect (at 8.7 -1.4) (size 1.45 0.2) (layers "F.Cu" "F.Paste" "F.Mask")
       (net 21 "/BRAINS/~{MREQ}") (pinfunction "IO") (pintype "bidirectional"))
@@
     (fp_line (start -2.2 3.25) (end -2.2 -2.25) (layer "F.Fab") (width 0.1))
     (pad "1" smd roundrect (at -2.8625 -2.925) (size 1.475 0.4) (layers "F.Cu" "F.Paste" "F.Mask") (roundrect_rratio 0.25)
-      (net 2 "GND") (pinfunction "A->B") (pintype "input"))
+      (net 236 "/BRAINS/DIR") (pinfunction "A->B") (pintype "input"))
     (pad "2" smd roundrect (at -2.8625 -2.275) (size 1.475 0.4) (layers "F.Cu" "F.Paste" "F.Mask") (roundrect_rratio 0.25)
       (net 53 "/BRAINS/EDB0") (pinfunction "A0") (pintype "tri_state"))
